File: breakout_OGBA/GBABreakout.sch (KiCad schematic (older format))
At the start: 17 parts, among them J1 Conn_01x16

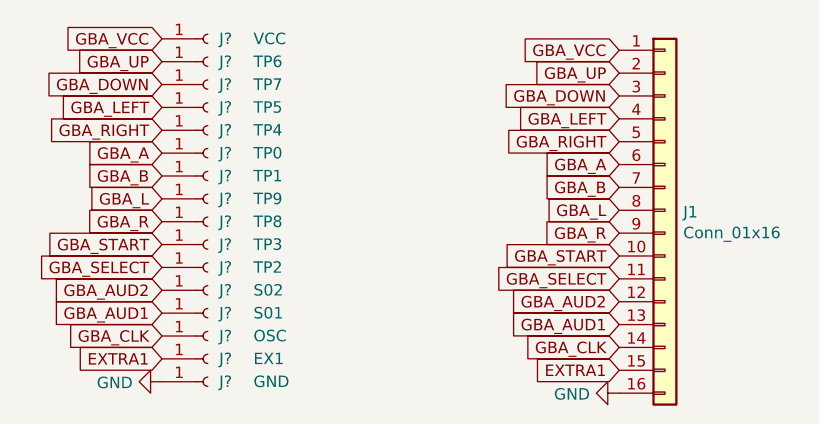
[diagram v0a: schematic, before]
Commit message: Major Updates
* Added QSB for GBA SP
* Fixed wrong supply voltare for Components in case of SP setup
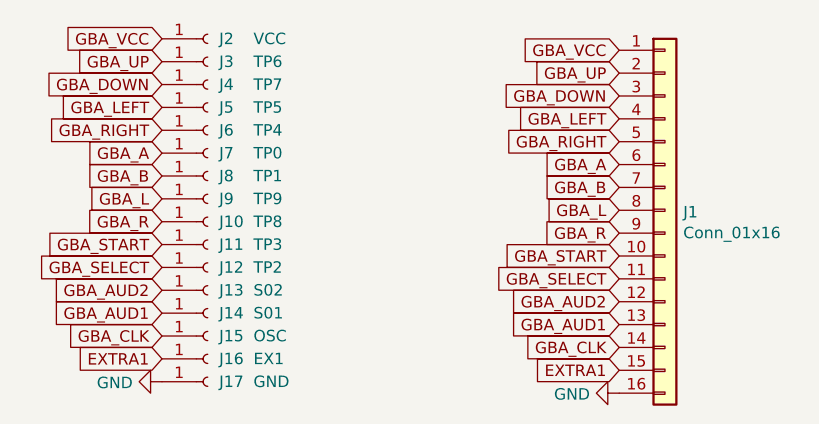
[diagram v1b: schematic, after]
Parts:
- J10, J11, J12, J13, J14, J15, J16, J17, J2, J3, J4, J5, J6, J7, J8, J9: renamed from J?; footprint (none) -> OFFSET:SOLDER_PAD
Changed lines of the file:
@@
 $EndComp
 $Comp
-L Connector:Conn_01x01_Female J?
+L Connector:Conn_01x01_Female J2
 U 1 1 6011B727
 P 3000 1400
-F 0 "J?" H 3050 1400 50  0000 L CNN
+F 0 "J2" H 3050 1400 50  0000 L CNN
 F 1 "VCC" H 3200 1400 50  0000 L CNN
-F 2 "" H 3000 1400 50  0001 C CNN
+F 2 "OFFSET:SOLDER_PAD" H 3000 1400 50  0001 C CNN
 F 3 "~" H 3000 1400 50  0001 C CNN
 	1    3000 1400
@@
 $EndComp
 $Comp
-L Connector:Conn_01x01_Female J?
+L Connector:Conn_01x01_Female J3
 U 1 1 6011BBB1
 P 3000 1500
-F 0 "J?" H 3050 1500 50  0000 L CNN
+F 0 "J3" H 3050 1500 50  0000 L CNN
 F 1 "TP6" H 3200 1500 50  0000 L CNN
-F 2 "" H 3000 1500 50  0001 C CNN
+F 2 "OFFSET:SOLDER_PAD" H 3000 1500 50  0001 C CNN
 F 3 "~" H 3000 1500 50  0001 C CNN
 	1    3000 1500
@@
 $EndComp
 $Comp
-L Connector:Conn_01x01_Female J?
+L Connector:Conn_01x01_Female J4
 U 1 1 6011C5F6
 P 3000 1600
-F 0 "J?" H 3050 1600 50  0000 L CNN
+F 0 "J4" H 3050 1600 50  0000 L CNN
 F 1 "TP7" H 3200 1600 50  0000 L CNN
-F 2 "" H 3000 1600 50  0001 C CNN
+F 2 "OFFSET:SOLDER_PAD" H 3000 1600 50  0001 C CNN
 F 3 "~" H 3000 1600 50  0001 C CNN
 	1    3000 1600
@@
 $EndComp
 $Comp
-L Connector:Conn_01x01_Female J?
+L Connector:Conn_01x01_Female J5
 U 1 1 6011C5FC
 P 3000 1700
-F 0 "J?" H 3050 1700 50  0000 L CNN
+F 0 "J5" H 3050 1700 50  0000 L CNN
 F 1 "TP5" H 3200 1700 50  0000 L CNN
-F 2 "" H 3000 1700 50  0001 C CNN
+F 2 "OFFSET:SOLDER_PAD" H 3000 1700 50  0001 C CNN
 F 3 "~" H 3000 1700 50  0001 C CNN
 	1    3000 1700
@@
 $EndComp
 $Comp
-L Connector:Conn_01x01_Female J?
+L Connector:Conn_01x01_Female J6
 U 1 1 6011CA16
 P 3000 1800
-F 0 "J?" H 3050 1800 50  0000 L CNN
+F 0 "J6" H 3050 1800 50  0000 L CNN
 F 1 "TP4" H 3200 1800 50  0000 L CNN
-F 2 "" H 3000 1800 50  0001 C CNN
+F 2 "OFFSET:SOLDER_PAD" H 3000 1800 50  0001 C CNN
 F 3 "~" H 3000 1800 50  0001 C CNN
 	1    3000 1800
@@
 $EndComp
 $Comp
-L Connector:Conn_01x01_Female J?
+L Connector:Conn_01x01_Female J7
 U 1 1 6011CA1C
 P 3000 1900
-F 0 "J?" H 3050 1900 50  0000 L CNN
+F 0 "J7" H 3050 1900 50  0000 L CNN
 F 1 "TP0" H 3200 1900 50  0000 L CNN
-F 2 "" H 3000 1900 50  0001 C CNN
+F 2 "OFFSET:SOLDER_PAD" H 3000 1900 50  0001 C CNN
 F 3 "~" H 3000 1900 50  0001 C CNN
 	1    3000 1900
@@
 $EndComp
 $Comp
-L Connector:Conn_01x01_Female J?
+L Connector:Conn_01x01_Female J8
 U 1 1 6011F8BE
 P 3000 2000
-F 0 "J?" H 3050 2000 50  0000 L CNN
+F 0 "J8" H 3050 2000 50  0000 L CNN
 F 1 "TP1" H 3200 2000 50  0000 L CNN
-F 2 "" H 3000 2000 50  0001 C CNN
+F 2 "OFFSET:SOLDER_PAD" H 3000 2000 50  0001 C CNN
 F 3 "~" H 3000 2000 50  0001 C CNN
 	1    3000 2000
@@
 $EndComp
 $Comp
-L Connector:Conn_01x01_Female J?
+L Connector:Conn_01x01_Female J9
 U 1 1 6011F8C4
 P 3000 2100
-F 0 "J?" H 3050 2100 50  0000 L CNN
+F 0 "J9" H 3050 2100 50  0000 L CNN
 F 1 "TP9" H 3200 2100 50  0000 L CNN
-F 2 "" H 3000 2100 50  0001 C CNN
+F 2 "OFFSET:SOLDER_PAD" H 3000 2100 50  0001 C CNN
 F 3 "~" H 3000 2100 50  0001 C CNN
 	1    3000 2100
@@
 $EndComp
 $Comp
-L Connector:Conn_01x01_Female J?
+L Connector:Conn_01x01_Female J10
 U 1 1 6011F8CA
 P 3000 2200
-F 0 "J?" H 3050 2200 50  0000 L CNN
+F 0 "J10" H 3050 2200 50  0000 L CNN
 F 1 "TP8" H 3200 2200 50  0000 L CNN
-F 2 "" H 3000 2200 50  0001 C CNN
+F 2 "OFFSET:SOLDER_PAD" H 3000 2200 50  0001 C CNN
 F 3 "~" H 3000 2200 50  0001 C CNN
 	1    3000 2200
@@
 $EndComp
 $Comp
-L Connector:Conn_01x01_Female J?
+L Connector:Conn_01x01_Female J11
 U 1 1 6011F8D0
 P 3000 2300
-F 0 "J?" H 3050 2300 50  0000 L CNN
+F 0 "J11" H 3050 2300 50  0000 L CNN
 F 1 "TP3" H 3200 2300 50  0000 L CNN
-F 2 "" H 3000 2300 50  0001 C CNN
+F 2 "OFFSET:SOLDER_PAD" H 3000 2300 50  0001 C CNN
 F 3 "~" H 3000 2300 50  0001 C CNN
 	1    3000 2300
@@
 $EndComp
 $Comp
-L Connector:Conn_01x01_Female J?
+L Connector:Conn_01x01_Female J12
 U 1 1 6011F8D6
 P 3000 2400
-F 0 "J?" H 3050 2400 50  0000 L CNN
+F 0 "J12" H 3050 2400 50  0000 L CNN
 F 1 "TP2" H 3200 2400 50  0000 L CNN
-F 2 "" H 3000 2400 50  0001 C CNN
+F 2 "OFFSET:SOLDER_PAD" H 3000 2400 50  0001 C CNN
 F 3 "~" H 3000 2400 50  0001 C CNN
 	1    3000 2400
@@
 $EndComp
 $Comp
-L Connector:Conn_01x01_Female J?
+L Connector:Conn_01x01_Female J13
 U 1 1 6011F8DC
 P 3000 2500
-F 0 "J?" H 3050 2500 50  0000 L CNN
+F 0 "J13" H 3050 2500 50  0000 L CNN
 F 1 "S02" H 3200 2500 50  0000 L CNN
-F 2 "" H 3000 2500 50  0001 C CNN
+F 2 "OFFSET:SOLDER_PAD" H 3000 2500 50  0001 C CNN
 F 3 "~" H 3000 2500 50  0001 C CNN
 	1    3000 2500
@@
 $EndComp
 $Comp
-L Connector:Conn_01x01_Female J?
+L Connector:Conn_01x01_Female J14
 U 1 1 6012372C
 P 3000 2600
-F 0 "J?" H 3050 2600 50  0000 L CNN
+F 0 "J14" H 3050 2600 50  0000 L CNN
 F 1 "S01" H 3200 2600 50  0000 L CNN
-F 2 "" H 3000 2600 50  0001 C CNN
+F 2 "OFFSET:SOLDER_PAD" H 3000 2600 50  0001 C CNN
 F 3 "~" H 3000 2600 50  0001 C CNN
 	1    3000 2600
@@
 $EndComp
 $Comp
-L Connector:Conn_01x01_Female J?
+L Connector:Conn_01x01_Female J15
 U 1 1 60123732
 P 3000 2700
-F 0 "J?" H 3050 2700 50  0000 L CNN
+F 0 "J15" H 3050 2700 50  0000 L CNN
 F 1 "OSC" H 3200 2700 50  0000 L CNN
-F 2 "" H 3000 2700 50  0001 C CNN
+F 2 "OFFSET:SOLDER_PAD" H 3000 2700 50  0001 C CNN
 F 3 "~" H 3000 2700 50  0001 C CNN
 	1    3000 2700
@@
 $EndComp
 $Comp
-L Connector:Conn_01x01_Female J?
+L Connector:Conn_01x01_Female J16
 U 1 1 60123738
 P 3000 2800
-F 0 "J?" H 3050 2800 50  0000 L CNN
+F 0 "J16" H 3050 2800 50  0000 L CNN
 F 1 "EX1" H 3200 2800 50  0000 L CNN
-F 2 "" H 3000 2800 50  0001 C CNN
+F 2 "OFFSET:SOLDER_PAD" H 3000 2800 50  0001 C CNN
 F 3 "~" H 3000 2800 50  0001 C CNN
 	1    3000 2800
@@
 $EndComp
 $Comp
-L Connector:Conn_01x01_Female J?
+L Connector:Conn_01x01_Female J17
 U 1 1 60123B7B
 P 3000 2900
-F 0 "J?" H 3050 2900 50  0000 L CNN
+F 0 "J17" H 3050 2900 50  0000 L CNN
 F 1 "GND" H 3200 2900 50  0000 L CNN
-F 2 "" H 3000 2900 50  0001 C CNN
+F 2 "OFFSET:SOLDER_PAD" H 3000 2900 50  0001 C CNN
 F 3 "~" H 3000 2900 50  0001 C CNN
 	1    3000 2900
